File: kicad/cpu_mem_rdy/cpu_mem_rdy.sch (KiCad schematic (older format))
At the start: 36 parts, among them P1 CONN_02X04, P3 CONN_01X03, P4 CONN_02X02, P6 POWER, SW1 SW_PUSH, U1 W65C02SP, U2 LM555N, U3 74HCT00, U4 74LS393, U6 28C256, U7 HM62256BLP-7, U8 HM62256BLP-7, X1 OSC

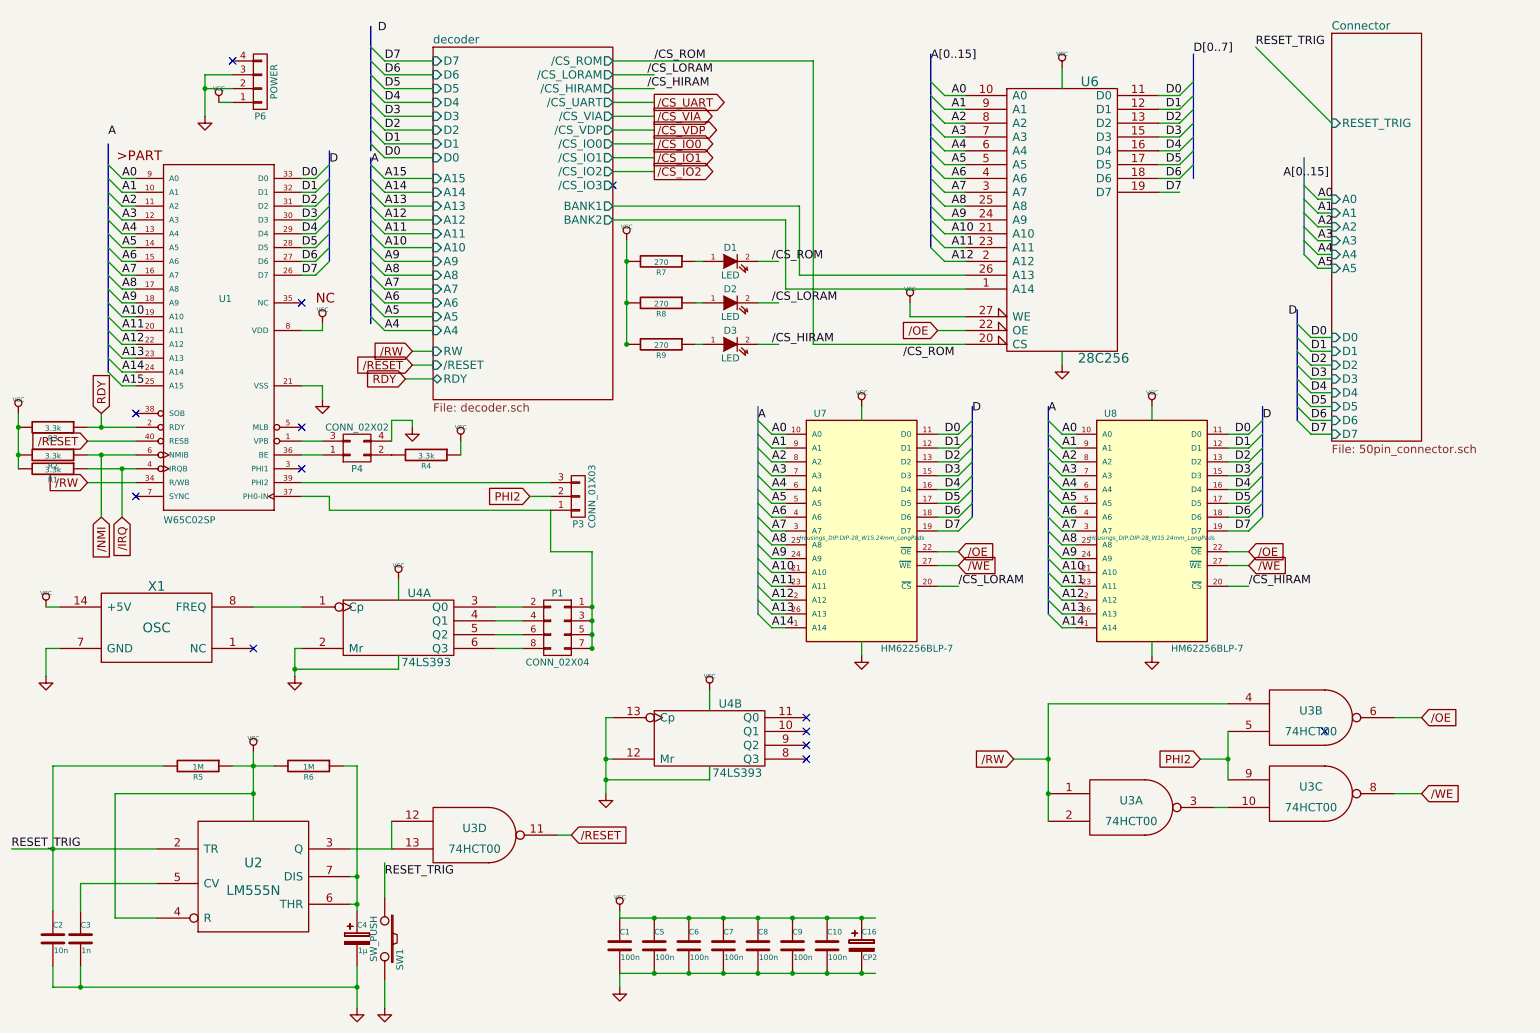
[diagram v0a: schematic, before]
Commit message: cleanup routing, micro usb jack
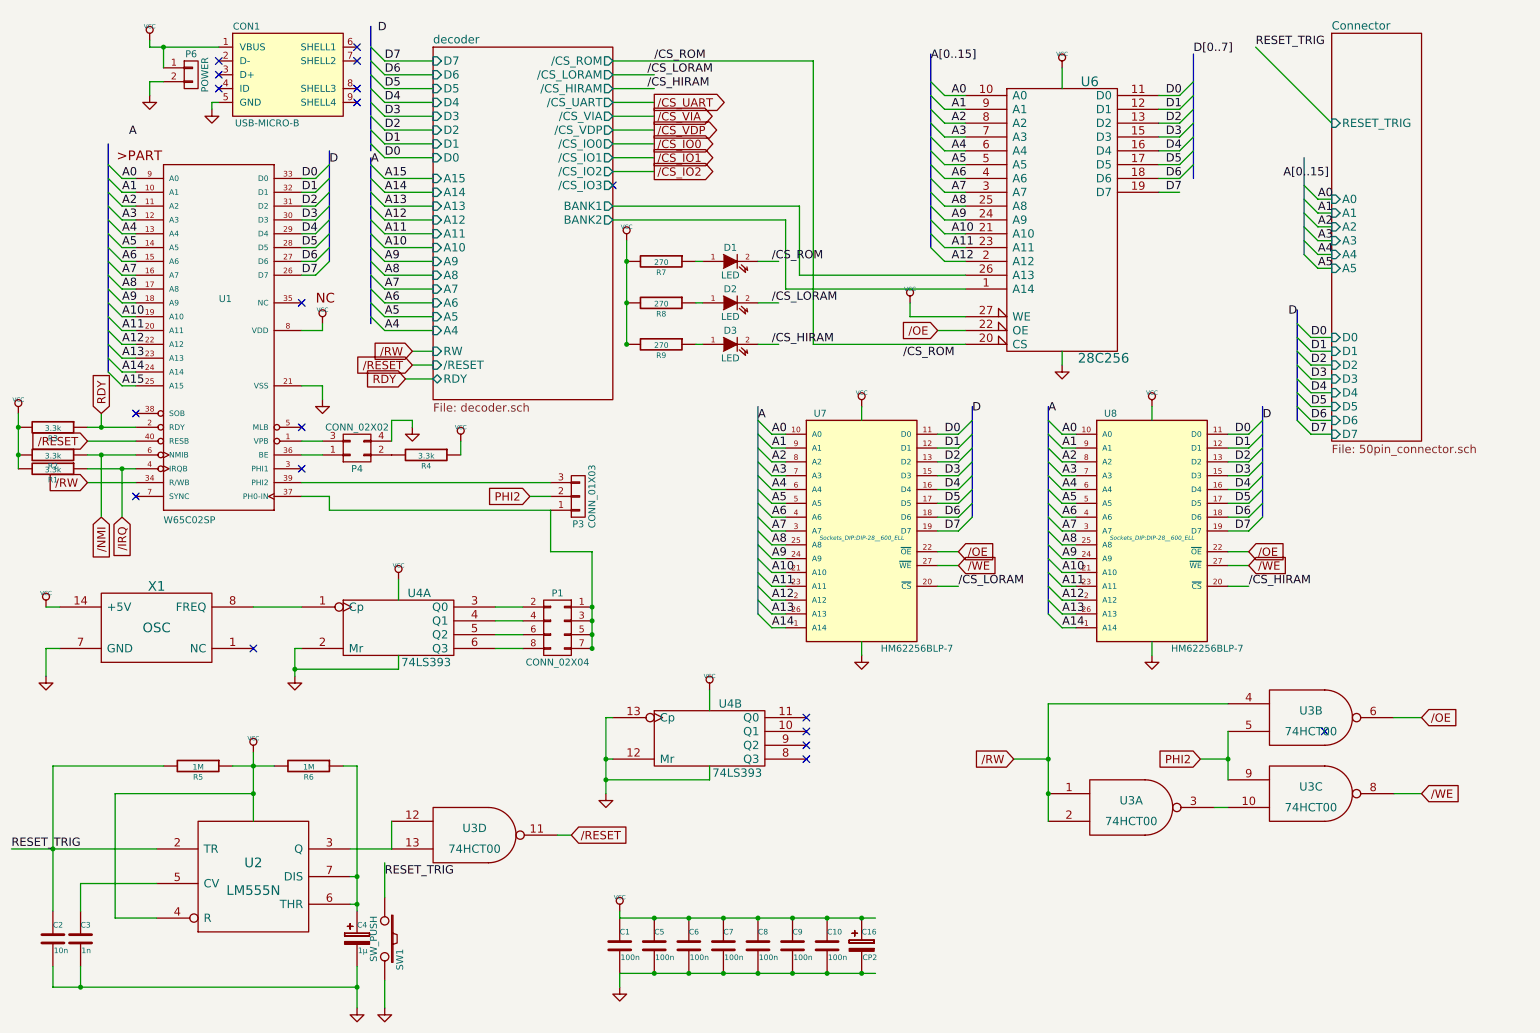
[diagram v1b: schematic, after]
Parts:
- removed P6: POWER, Pin_Headers:Pin_Header_Angled_1x04, symbol CONN_01X04
- added CON1: USB-MICRO-B, Connect:USB_Micro-B, symbol USB-MICRO-B
- added P6: POWER, Pin_Headers:Pin_Header_Straight_1x02, symbol CONN_01X02
- C1, C10, C2, C3, C5, C6, C7, C8, C9: footprint Capacitors_ThroughHole:C_Rect_L4_W2.5_P2.5 -> Discret:C1
- C16: footprint Capacitors_ThroughHole:C_Radial_D5_L11_P2.5 -> Capacitors_Elko_ThroughHole:Elko_vert_11.2x7.5mm_RM2.5
- C4: footprint Capacitors_ThroughHole:C_Radial_D5_L6_P2.5 -> Capacitors_Elko_ThroughHole:Elko_vert_DM5_RM2-5
- SW1: footprint Buttons_Switches_ThroughHole:SW_PUSH_SMALL -> Discret:PUSH_BUTT_SHAPE1
- U1: footprint Housings_DIP:DIP-40_W15.24mm_LongPads -> Sockets_DIP:DIP-40__600_ELL
- U2: footprint Housings_DIP:DIP-8_W7.62mm_LongPads -> Sockets_DIP:DIP-8__300_ELL
- U3, U4: footprint Housings_DIP:DIP-14_W7.62mm_LongPads -> Sockets_DIP:DIP-14__300_ELL
- U6, U7, U8: footprint Housings_DIP:DIP-28_W15.24mm_LongPads -> Sockets_DIP:DIP-28__600_ELL
- X1: footprint Oscillators:KXO-200_LargePads -> Oscillator-Modules:OSCILLATOR_KXO-200_LargePads
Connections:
- net GND: now also CON1.5 (GND), P6.2 (P2)
- net VCC: now also CON1.1 (VBUS), P6.1 (P1)
- no-connect marks 13 -> 19
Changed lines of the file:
@@
 LIBS:xo-14s
 LIBS:osc
+LIBS:cpu_mem_rdy-cache
 EELAYER 25 0
 EELAYER END
@@
 F 0 "U1" H 2000 2550 50  0000 L BNN
 F 1 "W65C02SP" H 1600 950 50  0000 L BNN
-F 2 "Housings_DIP:DIP-40_W15.24mm_LongPads" H 2000 2700 50  0001 C CNN
+F 2 "Sockets_DIP:DIP-40__600_ELL" H 2000 2700 50  0001 C CNN
 F 3 "" H 2000 2550 60  0000 C CNN
 	1    2000 2550
@@
 F 0 "U2" H 2250 6800 70  0000 C CNN
 F 1 "LM555N" H 2250 6600 70  0000 C CNN
-F 2 "Housings_DIP:DIP-8_W7.62mm_LongPads" H 2250 6700 60  0001 C CNN
+F 2 "Sockets_DIP:DIP-8__300_ELL" H 2250 6700 60  0001 C CNN
 F 3 "" H 2250 6700 60  0000 C CNN
 	1    2250 6700
@@
 F 0 "C1" H 4900 7300 40  0000 L CNN
 F 1 "100n" H 4906 7115 40  0000 L CNN
-F 2 "Capacitors_ThroughHole:C_Rect_L4_W2.5_P2.5" H 4938 7050 30  0001 C CNN
+F 2 "Discret:C1" H 4938 7050 30  0001 C CNN
 F 3 "" H 4900 7200 60  0000 C CNN
 	1    4900 7200
@@
 F 0 "C2" H 800 7250 40  0000 L CNN
 F 1 "10n" H 806 7065 40  0000 L CNN
-F 2 "Capacitors_ThroughHole:C_Rect_L4_W2.5_P2.5" H 838 7000 30  0001 C CNN
+F 2 "Discret:C1" H 838 7000 30  0001 C CNN
 F 3 "" H 800 7150 60  0000 C CNN
 	1    800  7150
@@
 F 0 "C3" H 1000 7250 40  0000 L CNN
 F 1 "1n" H 1006 7065 40  0000 L CNN
-F 2 "Capacitors_ThroughHole:C_Rect_L4_W2.5_P2.5" H 1038 7000 30  0001 C CNN
+F 2 "Discret:C1" H 1038 7000 30  0001 C CNN
 F 3 "" H 1000 7150 60  0000 C CNN
 	1    1000 7150
@@
 F 0 "C4" H 3000 7250 40  0000 L CNN
 F 1 "1µ" H 3006 7065 40  0000 L CNN
-F 2 "Capacitors_ThroughHole:C_Radial_D5_L6_P2.5" H 3038 7000 30  0001 C CNN
+F 2 "Capacitors_Elko_ThroughHole:Elko_vert_DM5_RM2-5" H 3038 7000 30  0001 C CNN
 F 3 "" H 3000 7150 60  0000 C CNN
 	1    3000 7150
@@
 F 0 "U3" H 3850 6450 60  0000 C CNN
 F 1 "74HCT00" H 3850 6300 60  0000 C CNN
-F 2 "Housings_DIP:DIP-14_W7.62mm_LongPads" H 3850 6400 60  0001 C CNN
+F 2 "Sockets_DIP:DIP-14__300_ELL" H 3850 6400 60  0001 C CNN
 F 3 "" H 3850 6400 60  0000 C CNN
 	4    3850 6400
@@
 F 0 "U4" H 3450 5150 60  0000 C CNN
 F 1 "74LS393" H 3500 4650 60  0000 C CNN
-F 2 "Housings_DIP:DIP-14_W7.62mm_LongPads" H 3300 4900 60  0001 C CNN
+F 2 "Sockets_DIP:DIP-14__300_ELL" H 3300 4900 60  0001 C CNN
 F 3 "" H 3300 4900 60  0000 C CNN
 	1    3300 4900
@@
 F 0 "C5" H 5150 7300 40  0000 L CNN
 F 1 "100n" H 5156 7115 40  0000 L CNN
-F 2 "Capacitors_ThroughHole:C_Rect_L4_W2.5_P2.5" H 5188 7050 30  0001 C CNN
+F 2 "Discret:C1" H 5188 7050 30  0001 C CNN
 F 3 "" H 5150 7200 60  0000 C CNN
 	1    5150 7200
@@
 F 0 "C6" H 5400 7300 40  0000 L CNN
 F 1 "100n" H 5406 7115 40  0000 L CNN
-F 2 "Capacitors_ThroughHole:C_Rect_L4_W2.5_P2.5" H 5438 7050 30  0001 C CNN
+F 2 "Discret:C1" H 5438 7050 30  0001 C CNN
 F 3 "" H 5400 7200 60  0000 C CNN
 	1    5400 7200
@@
 F 0 "C7" H 5650 7300 40  0000 L CNN
 F 1 "100n" H 5656 7115 40  0000 L CNN
-F 2 "Capacitors_ThroughHole:C_Rect_L4_W2.5_P2.5" H 5688 7050 30  0001 C CNN
+F 2 "Discret:C1" H 5688 7050 30  0001 C CNN
 F 3 "" H 5650 7200 60  0000 C CNN
 	1    5650 7200
@@
 F 0 "U3" H 8600 6250 60  0000 C CNN
 F 1 "74HCT00" H 8600 6100 60  0000 C CNN
-F 2 "Housings_DIP:DIP-14_W7.62mm_LongPads" H 8600 6200 60  0001 C CNN
+F 2 "Sockets_DIP:DIP-14__300_ELL" H 8600 6200 60  0001 C CNN
 F 3 "" H 8600 6200 60  0000 C CNN
 	1    8600 6200
@@
 F 0 "U3" H 9900 5600 60  0000 C CNN
 F 1 "74HCT00" H 9900 5450 60  0000 C CNN
-F 2 "Housings_DIP:DIP-14_W7.62mm_LongPads" H 9900 5550 60  0001 C CNN
+F 2 "Sockets_DIP:DIP-14__300_ELL" H 9900 5550 60  0001 C CNN
 F 3 "" H 9900 5550 60  0000 C CNN
 	2    9900 5550
@@
 F 0 "U3" H 9900 6150 60  0000 C CNN
 F 1 "74HCT00" H 9900 6000 60  0000 C CNN
-F 2 "Housings_DIP:DIP-14_W7.62mm_LongPads" H 9900 6100 60  0001 C CNN
+F 2 "Sockets_DIP:DIP-14__300_ELL" H 9900 6100 60  0001 C CNN
 F 3 "" H 9900 6100 60  0000 C CNN
 	3    9900 6100
@@
 F 0 "C8" H 5900 7300 40  0000 L CNN
 F 1 "100n" H 5906 7115 40  0000 L CNN
-F 2 "Capacitors_ThroughHole:C_Rect_L4_W2.5_P2.5" H 5938 7050 30  0001 C CNN
+F 2 "Discret:C1" H 5938 7050 30  0001 C CNN
 F 3 "" H 5900 7200 60  0000 C CNN
 	1    5900 7200
@@
 F 0 "U7" H 6350 5150 50  0000 C CNN
 F 1 "HM62256BLP-7" H 7050 3450 50  0000 C CNN
-F 2 "Housings_DIP:DIP-28_W15.24mm_LongPads" H 6650 4250 30  0000 C CIN
+F 2 "Sockets_DIP:DIP-28__600_ELL" H 6650 4250 30  0000 C CIN
 F 3 "" H 6650 4250 60  0000 C CNN
 	1    6650 4250
@@
 F 0 "C9" H 6150 7300 40  0000 L CNN
 F 1 "100n" H 6156 7115 40  0000 L CNN
-F 2 "Capacitors_ThroughHole:C_Rect_L4_W2.5_P2.5" H 6188 7050 30  0001 C CNN
+F 2 "Discret:C1" H 6188 7050 30  0001 C CNN
 F 3 "" H 6150 7200 60  0000 C CNN
 	1    6150 7200
@@
 F 0 "C10" H 6400 7300 40  0000 L CNN
 F 1 "100n" H 6406 7115 40  0000 L CNN
-F 2 "Capacitors_ThroughHole:C_Rect_L4_W2.5_P2.5" H 6438 7050 30  0001 C CNN
+F 2 "Discret:C1" H 6438 7050 30  0001 C CNN
 F 3 "" H 6400 7200 60  0000 C CNN
 	1    6400 7200
@@
 F 0 "SW1" H 3350 7260 50  0000 C CNN
 F 1 "SW_PUSH" H 3200 7070 50  0000 C CNN
-F 2 "Buttons_Switches_ThroughHole:SW_PUSH_SMALL" H 3200 7150 60  0001 C CNN
+F 2 "Discret:PUSH_BUTT_SHAPE1" H 3200 7150 60  0001 C CNN
 F 3 "" H 3200 7150 60  0000 C CNN
 	1    3200 7150
@@
 F 0 "U8" H 8450 5150 50  0000 C CNN
 F 1 "HM62256BLP-7" H 9150 3450 50  0000 C CNN
-F 2 "Housings_DIP:DIP-28_W15.24mm_LongPads" H 8750 4250 30  0000 C CIN
+F 2 "Sockets_DIP:DIP-28__600_ELL" H 8750 4250 30  0000 C CIN
 F 3 "" H 8750 4250 60  0000 C CNN
 	1    8750 4250
@@
 Text Label 8000 3350 0    60   ~ 0
 A
-Text Label 1200 1350 0    60   ~ 0
+Text Label 1350 1350 0    60   ~ 0
 A
 Text Label 2800 1550 0    60   ~ 0
@@
 F 0 "X1" H 1550 5200 70  0000 C CNN
 F 1 "OSC" H 1550 4900 70  0000 C CNN
-F 2 "Oscillators:KXO-200_LargePads" H 1550 4900 60  0001 C CNN
+F 2 "Oscillator-Modules:OSCILLATOR_KXO-200_LargePads" H 1550 4900 60  0001 C CNN
 F 3 "" H 1550 4900 60  0000 C CNN
 	1    1550 4900
@@
 F 0 "U6" H 8300 2950 70  0000 C CNN
 F 1 "28C256" H 8400 950 70  0000 C CNN
-F 2 "Housings_DIP:DIP-28_W15.24mm_LongPads" H 8100 1950 60  0001 C CNN
+F 2 "Sockets_DIP:DIP-28__600_ELL" H 8100 1950 60  0001 C CNN
 F 3 "" H 8100 1950 60  0000 C CNN
 	1    8100 1950
@@
 F 0 "C16" H 6650 7300 40  0000 L CNN
 F 1 "CP2" H 6656 7115 40  0000 L CNN
-F 2 "Capacitors_ThroughHole:C_Radial_D5_L11_P2.5" H 6688 7050 30  0001 C CNN
+F 2 "Capacitors_Elko_ThroughHole:Elko_vert_11.2x7.5mm_RM2.5" H 6688 7050 30  0001 C CNN
 F 3 "" H 6650 7200 60  0000 C CNN
 	1    6650 7200
@@
 F 0 "U4" H 5700 5950 60  0000 C CNN
 F 1 "74LS393" H 5750 5450 60  0000 C CNN
-F 2 "Housings_DIP:DIP-14_W7.62mm_LongPads" H 5550 5700 60  0001 C CNN
+F 2 "Sockets_DIP:DIP-14__300_ELL" H 5550 5700 60  0001 C CNN
 F 3 "" H 5550 5700 60  0000 C CNN
 	2    5550 5700
@@
 	8750 3300 8750 3400
 $Comp
-L CONN_01X04 P6
-U 1 1 54B57D9B
-P 2300 950
-F 0 "P6" H 2300 1200 50  0000 C CNN
-F 1 "POWER" V 2400 950 50  0000 C CNN
-F 2 "Pin_Headers:Pin_Header_Angled_1x04" H 2300 950 60  0001 C CNN
-F 3 "" H 2300 950 60  0000 C CNN
-	1    2300 950
-	1    0    0    1
-$EndComp
-$Comp
-L VCC #PWR024
-U 1 1 54B581D7
-P 2000 1100
-F 0 "#PWR024" H 2000 1200 30  0001 C CNN
-F 1 "VCC" H 2000 1200 30  0000 C CNN
-F 2 "" H 2000 1100 60  0000 C CNN
-F 3 "" H 2000 1100 60  0000 C CNN
-	1    2000 1100
-	1    0    0    -1
-$EndComp
-$Comp
-L GND #PWR025
+L GND #PWR024
 U 1 1 54B5858D
-P 1900 1200
-F 0 "#PWR025" H 1900 1200 30  0001 C CNN
-F 1 "GND" H 1900 1130 30  0001 C CNN
-F 2 "" H 1900 1200 60  0000 C CNN
-F 3 "" H 1900 1200 60  0000 C CNN
-	1    1900 1200
-	1    0    0    -1
-$EndComp
-Wire Wire Line
-	2100 900  1900 900
-Wire Wire Line
-	1900 900  1900 1200
-Wire Wire Line
-	2100 1000 1900 1000
-Connection ~ 1900 1000
+P 1500 1050
+F 0 "#PWR024" H 1500 1050 30  0001 C CNN
+F 1 "GND" H 1500 980 30  0001 C CNN
+F 2 "" H 1500 1050 60  0000 C CNN
+F 3 "" H 1500 1050 60  0000 C CNN
+	1    1500 1050
+	1    0    0    -1
+$EndComp
+Wire Wire Line
+	1600 950  1500 950
+Wire Wire Line
+	1500 950  1500 1050
 $Comp
 L LED D1
@@
 	4950 2100 4950 2850
 $Comp
-L VCC #PWR026
+L VCC #PWR025
 U 1 1 54C3BFBB
 P 4950 2100
-F 0 "#PWR026" H 4950 2200 30  0001 C CNN
+F 0 "#PWR025" H 4950 2200 30  0001 C CNN
 F 1 "VCC" H 4950 2200 30  0000 C CNN
 F 2 "" H 4950 2100 60  0000 C CNN
@@
 Connection ~ 4950 2550
 Connection ~ 4950 2850
-NoConn ~ 2100 800
-Wire Wire Line
-	2000 1100 2100 1100
 Text GLabel 3350 3100 0    60   Input ~ 0
 RDY
@@
 F16 "RESET_TRIG" I L 10050 1250 60
 $EndSheet
+$Comp
+L USB-MICRO-B CON1
+U 1 1 56B0E071
+P 2500 900
+F 0 "CON1" H 2200 1250 50  0000 C CNN
+F 1 "USB-MICRO-B" H 2350 550 50  0000 C CNN
+F 2 "Connect:USB_Micro-B" H 2500 800 50  0001 C CNN
+F 3 "" H 2500 800 50  0000 C CNN
+	1    2500 900
+	1    0    0    -1
+$EndComp
+$Comp
+L GND #PWR026
+U 1 1 56B0EAD2
+P 1950 1150
+F 0 "#PWR026" H 1950 1150 30  0001 C CNN
+F 1 "GND" H 1950 1080 30  0001 C CNN
+F 2 "" H 1950 1150 60  0000 C CNN
+F 3 "" H 1950 1150 60  0000 C CNN
+	1    1950 1150
+	1    0    0    -1
+$EndComp
+Wire Wire Line
+	1950 1150 1950 1100
+Wire Wire Line
+	1950 1100 2000 1100
+$Comp
+L VCC #PWR027
+U 1 1 56B0EDB8
+P 1500 650
+F 0 "#PWR027" H 1500 750 30  0001 C CNN
+F 1 "VCC" H 1500 750 30  0000 C CNN
+F 2 "" H 1500 650 60  0000 C CNN
+F 3 "" H 1500 650 60  0000 C CNN
+	1    1500 650
+	1    0    0    -1
+$EndComp
+NoConn ~ 3000 700
+NoConn ~ 3000 800
+NoConn ~ 3000 1000
+NoConn ~ 3000 1100
+NoConn ~ 2000 800
+NoConn ~ 2000 900
+NoConn ~ 2000 1000
+$Comp
+L CONN_01X02 P6
+U 1 1 56B11104
+P 1800 900
+F 0 "P6" H 1800 1050 50  0000 C CNN
+F 1 "POWER" V 1900 900 50  0000 C CNN
+F 2 "Pin_Headers:Pin_Header_Straight_1x02" H 1800 900 60  0001 C CNN
+F 3 "" H 1800 900 60  0000 C CNN
+	1    1800 900
+	1    0    0    -1
+$EndComp
+Wire Wire Line
+	1600 850  1600 700
+Wire Wire Line
+	1500 700  2000 700
+Connection ~ 1600 700
+Wire Wire Line
+	1500 700  1500 650
 $EndSCHEMATC
